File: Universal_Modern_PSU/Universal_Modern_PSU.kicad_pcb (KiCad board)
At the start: 2 copper layers, 67 x 47 mm, 16 parts, among them J1 +12VDC Input, J2 Power Output, Q1 SUP53P06-20-E3, U1 DFR0831, U2 NKE1212SC, U3 R-78CK5.0-0.5

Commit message: Minor updates
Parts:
- C4: footprint Capacitor_THT:C_Radial_D5.0mm_H5.0mm_P2.00mm -> Capacitor_THT:C_Radial_D6.3mm_H7.0mm_P2.50mm
- moved C2 17.9 mm to (123.8, 106.4), turned to 0 degrees
- moved C3 13.3 mm to (139.0, 106.4), turned to 180 degrees
- moved C4 1.68 mm to (158.8, 97.4)
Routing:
- net /-5V_{OUT}: track 62.1 -> 65.0 mm
- net /+5V_{OUT}: track 20.4 -> 19.1 mm

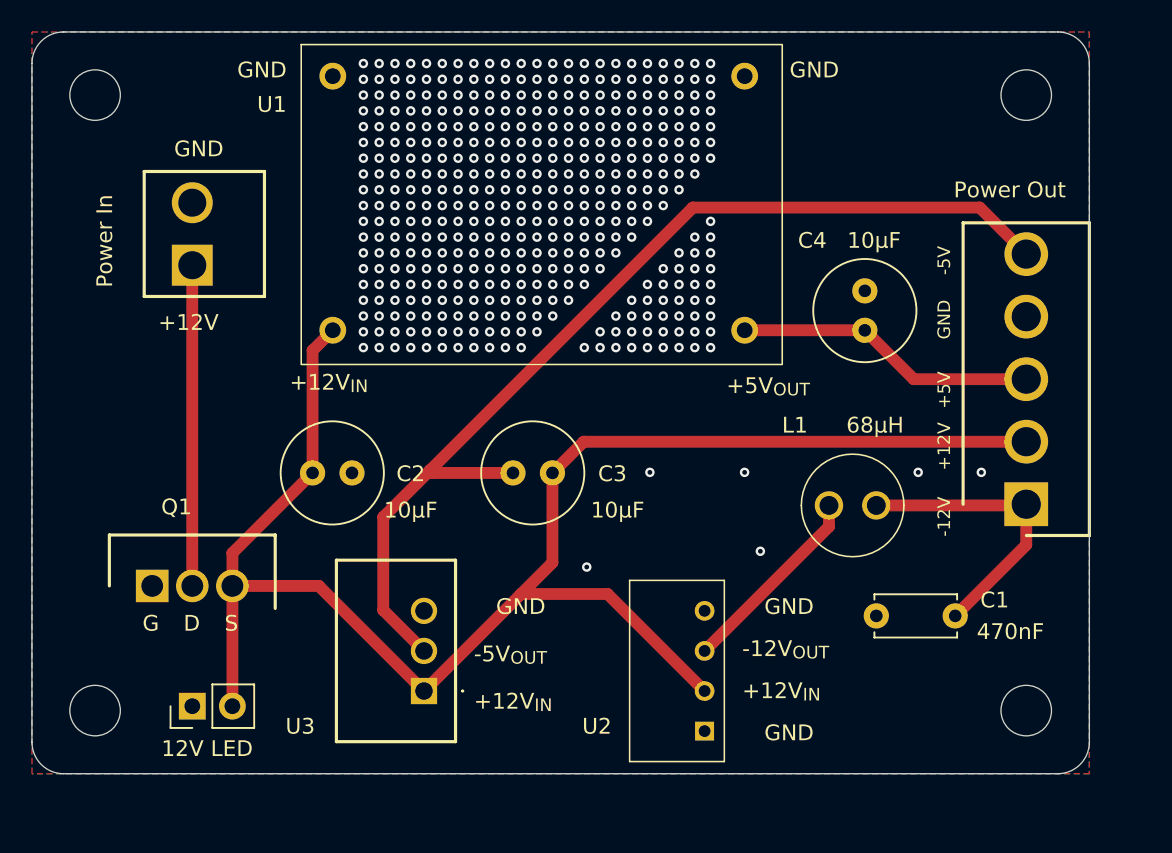
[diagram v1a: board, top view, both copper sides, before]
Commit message: Added additional capacitors
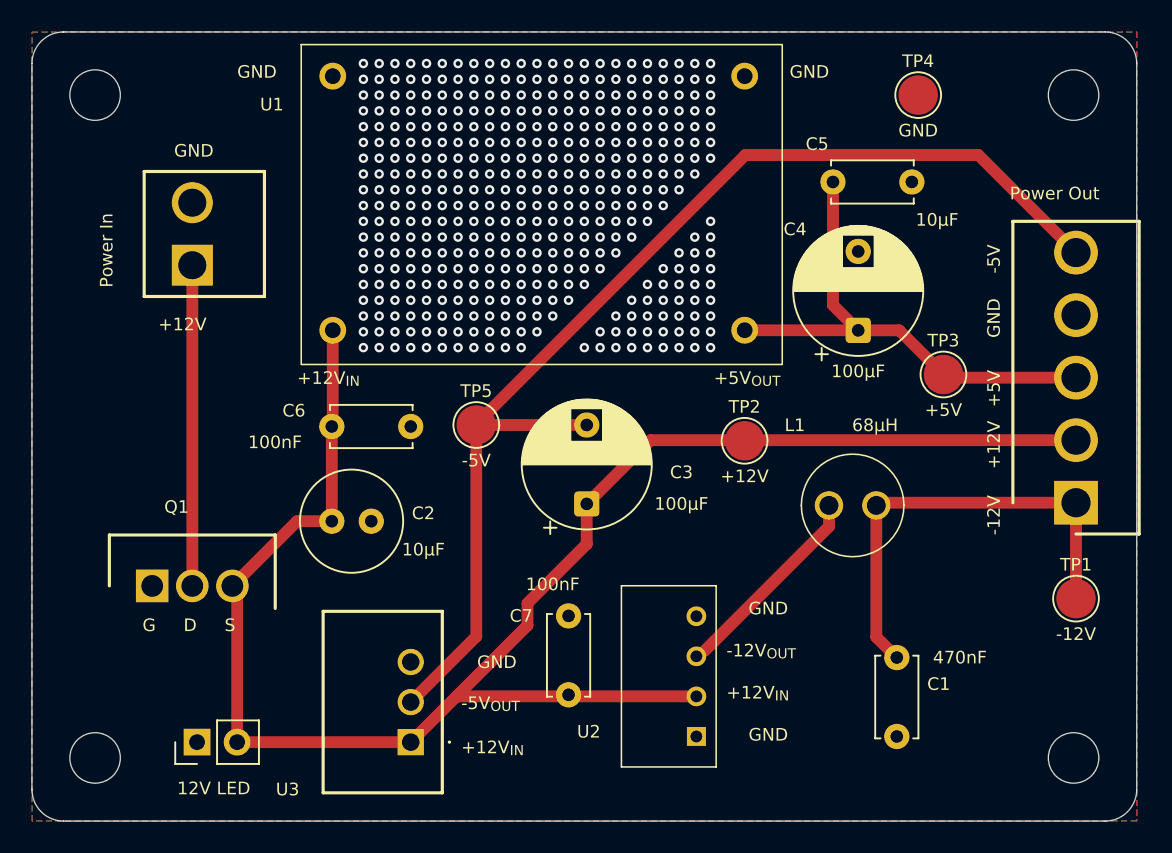
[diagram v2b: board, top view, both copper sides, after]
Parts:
- added C5: 10µF, Capacitor_THT:C_Disc_D5.0mm_W2.5mm_P5.00mm, F.Cu at (161.8, 88.0)
- added C6: 100nF, Capacitor_THT:C_Disc_D5.0mm_W2.5mm_P5.00mm, F.Cu at (125.0, 103.5)
- added C7: 100nF, Capacitor_THT:C_Disc_D5.0mm_W2.5mm_P5.00mm, F.Cu at (140.0, 115.5)
- added TP1: -12V, TestPoint:TestPoint_Pad_D2.5mm, F.Cu at (172.2, 114.4)
- added TP2: +12V, TestPoint:TestPoint_Pad_D2.5mm, F.Cu at (151.2, 104.4)
- added TP3: +5V, TestPoint:TestPoint_Pad_D2.5mm, F.Cu at (163.8, 100.2)
- added TP4: GND, TestPoint:TestPoint_Pad_D2.5mm, F.Cu at (162.2, 82.5)
- added TP5: -5V, TestPoint:TestPoint_Pad_D2.5mm, F.Cu at (134.2, 103.4)
- C3, C4: value 10µF -> 100µF; footprint Capacitor_THT:C_Radial_D6.3mm_H7.0mm_P2.50mm -> Capacitor_THT:CP_Radial_D8.0mm_P5.00mm
- moved C1 7.75 mm to (160.8, 123.1), turned to 90 degrees
- moved H2 4.24 mm to (172.0, 124.5)
- moved U3 3.35 mm to (130.0, 123.5)
- moved C2 3.29 mm to (125.0, 109.5)
- moved J2 3.16 mm to (172.2, 108.3)
- moved H1 3.00 mm to (172.0, 82.5)
- moved H3 3.00 mm to (110.0, 124.5)
- moved C3 2.93 mm to (141.2, 108.4), turned to 90 degrees
- moved D1 2.30 mm to (116.5, 123.5)
- moved U2 0.62 mm to (148.1, 123.1)
- moved C4 0.42 mm to (158.4, 97.4)
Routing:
- net /+5V_{OUT}: track 19.1 -> 32.3 mm
- net /-12V_{OUT}: track 18.5 -> 29.0 mm
- net /-5V_{OUT}: track 65.0 -> 74.0 mm
- net /+12V_{OUT}: track 103.6 -> 109.2 mm
- net /GND: vias 410 -> 404
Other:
- board size 67 x 47 mm -> 70 x 50 mm
